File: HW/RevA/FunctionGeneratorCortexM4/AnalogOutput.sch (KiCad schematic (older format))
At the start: 36 parts, among them U11 LTC6910, U12 TL072, U13 TL072, U4 SN74LVC1G3157DCKR

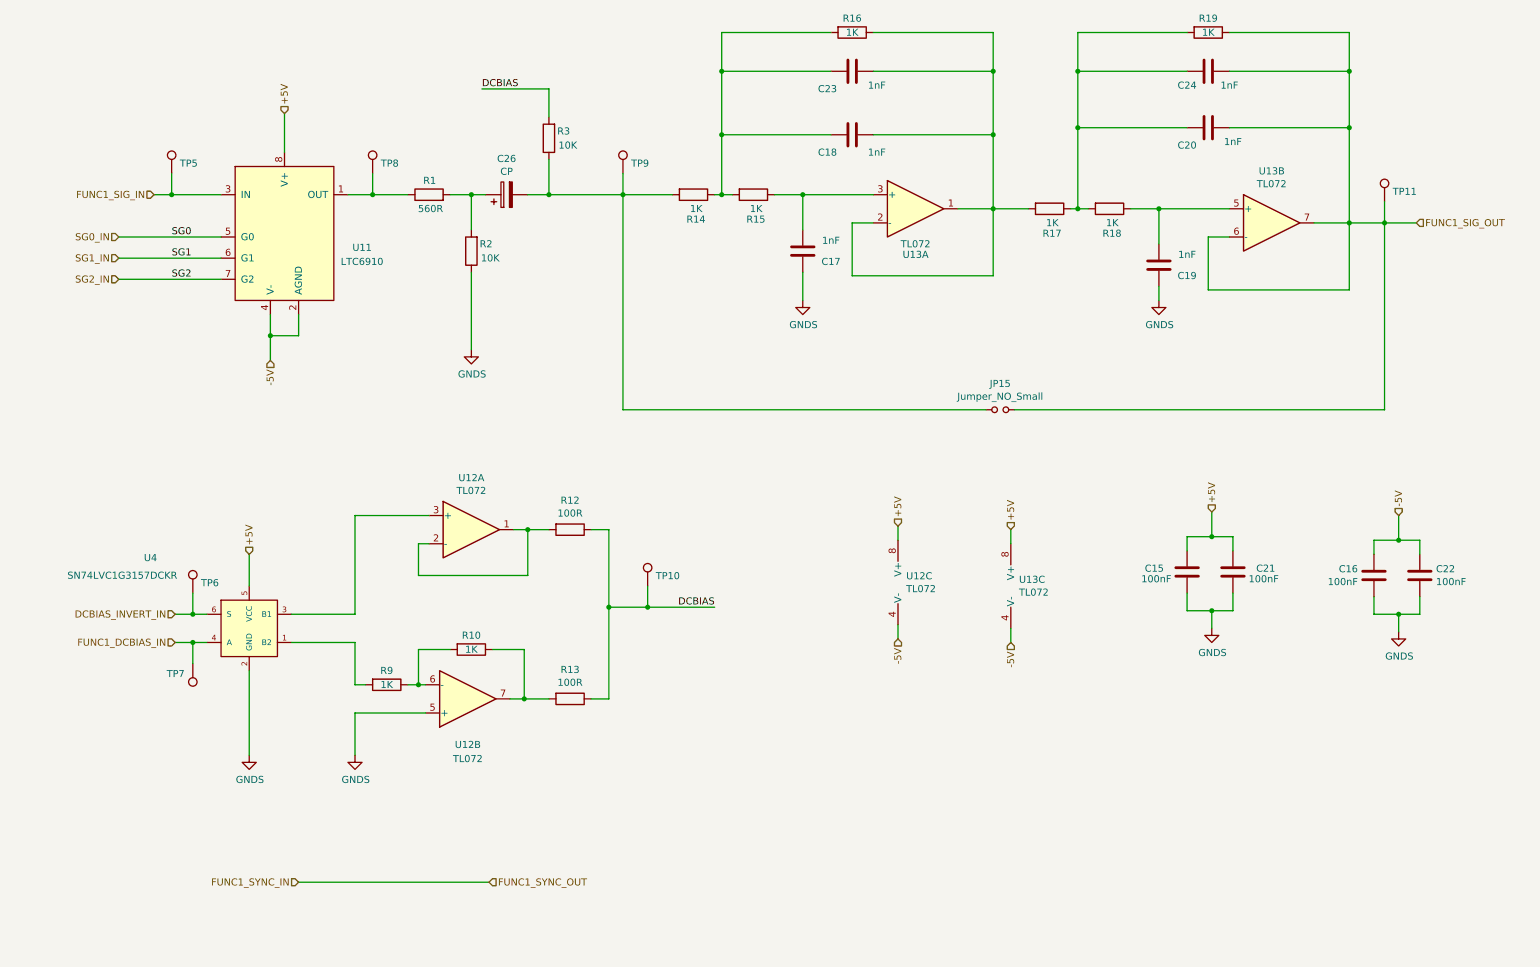
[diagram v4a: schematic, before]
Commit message: Finished RevA Layout
Dummy STMCubeMX project included in SW dir
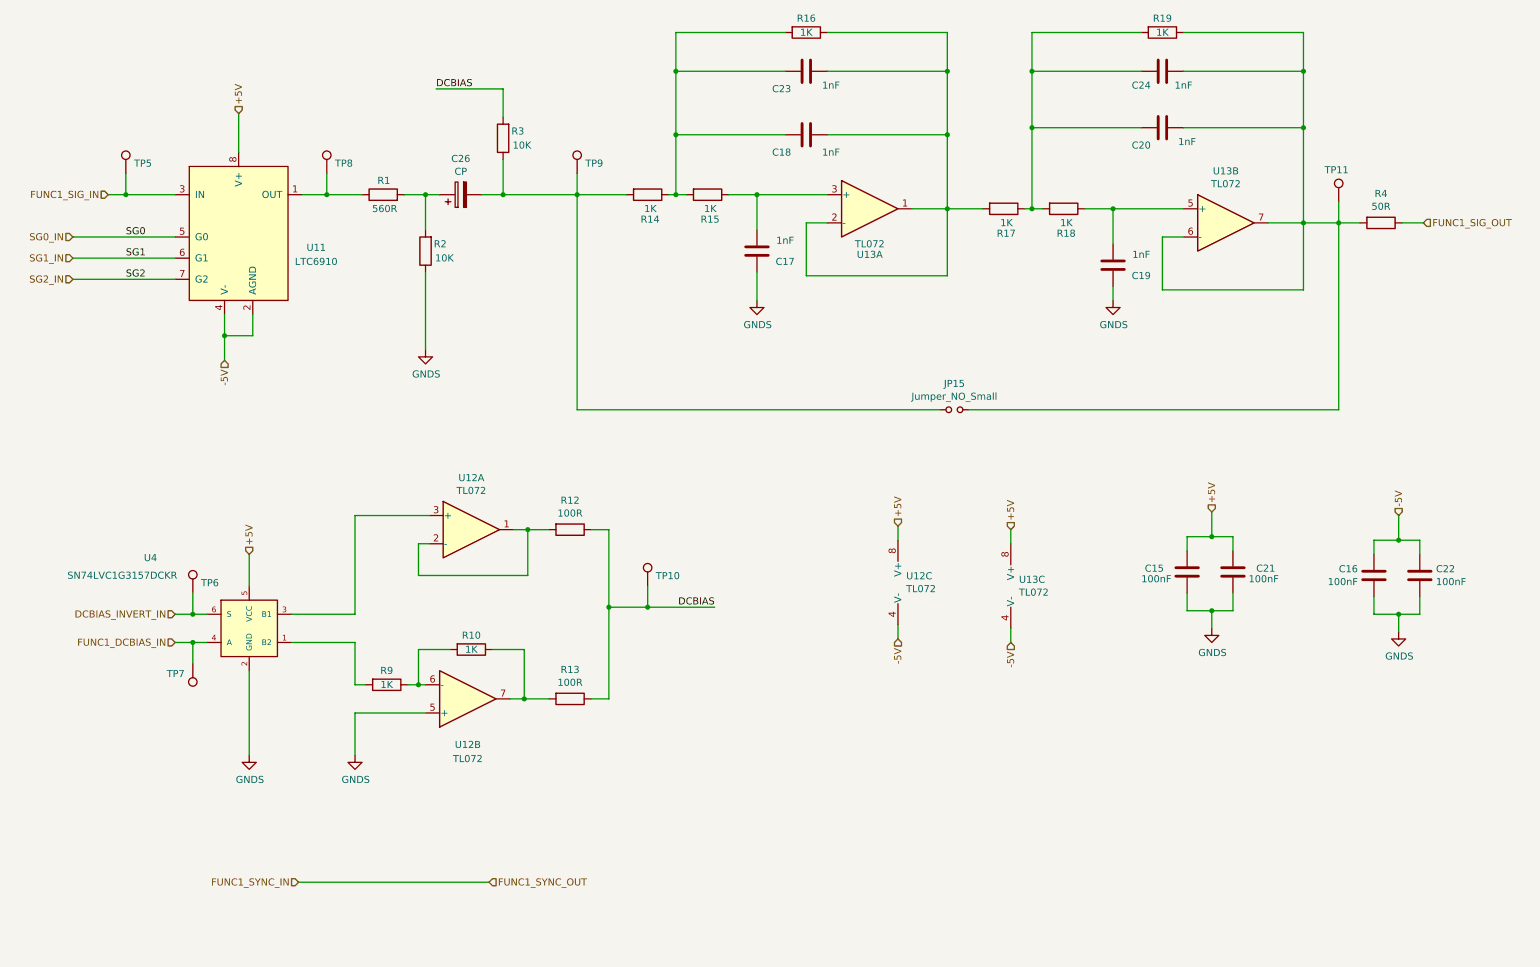
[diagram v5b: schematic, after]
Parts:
- added R4: 50R, Resistor_SMD:R_1206_3216Metric_Pad1.42x1.75mm_HandSolder, symbol Device:R
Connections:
- net FUNC1_SIG_OUT: now also R4.1; no longer C20.1, C24.1, JP15.2, R19.1, TP11.1, U13.6 (-), U13.7
- new net: C20.1, C24.1, JP15.2, R19.1, R4.2, TP11.1, U13.6 (-), U13.7
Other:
- moved on the sheet: C17, C18, C19, C20, C23, C24, C26, JP15, R1, R14, R15, R16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

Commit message: updated RevA
Generated GERBERS
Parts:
- added C9: 10uF, Capacitor_SMD:CP_Elec_4x5.7, symbol Device:CP
- added R21: 50R, Resistor_SMD:R_1206_3216Metric_Pad1.42x1.75mm_HandSolder, symbol Device:R
- added U7: MCP601-xOT, Package_TO_SOT_SMD:SOT-23-5, symbol Amplifier_Operational:MCP601-xOT
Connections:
- net +5V: now also U7.5 (V+)
- net FUNC1_SYNC_IN: now also C9.2
- net GNDS: now also U7.2 (V-)
- new net: R21.2, U7.1, U7.4 (-)
- new net: C9.1, U7.3 (+)
- new net FUNC1_SYNC_OUT: R21.1
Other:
- moved on the sheet: R10, R12, R13, R9, TP10, TP6, TP7, U12A, U12B, U4
